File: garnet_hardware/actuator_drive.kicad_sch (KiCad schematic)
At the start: 8 parts, among them J10 Conn_01x02_Pin, Q1 Q_NMOS, Q2 Q_NMOS, Q3 Q_NMOS, Q4 Q_NMOS

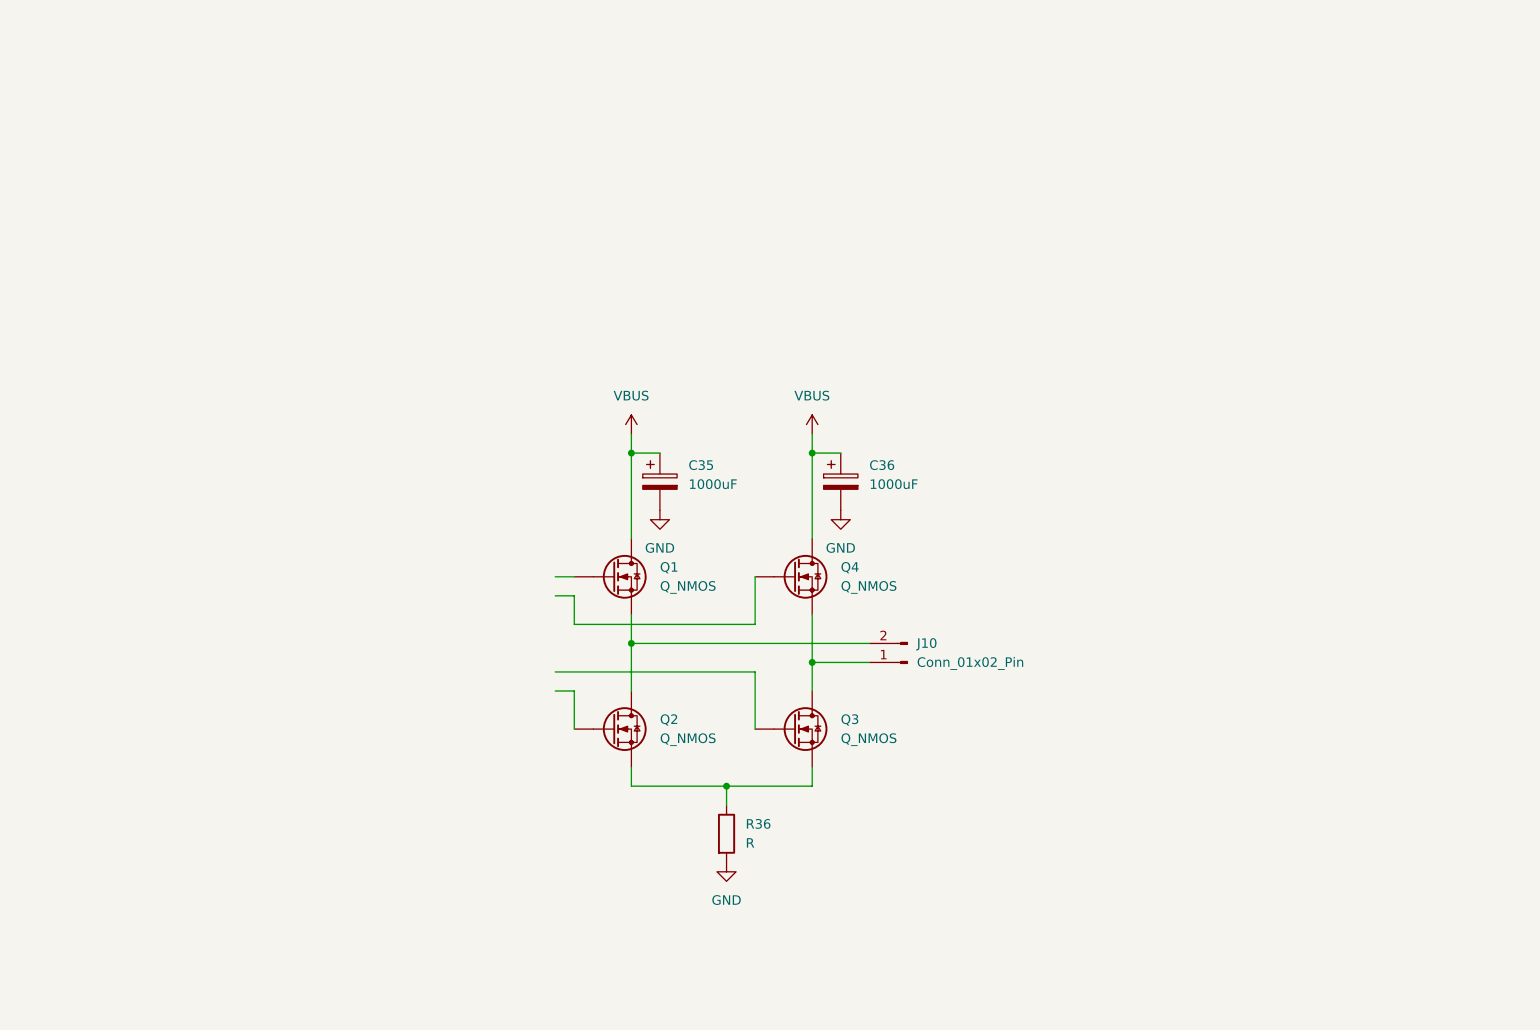
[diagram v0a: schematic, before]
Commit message: added part numbers for H-bridge, started on PCB layout
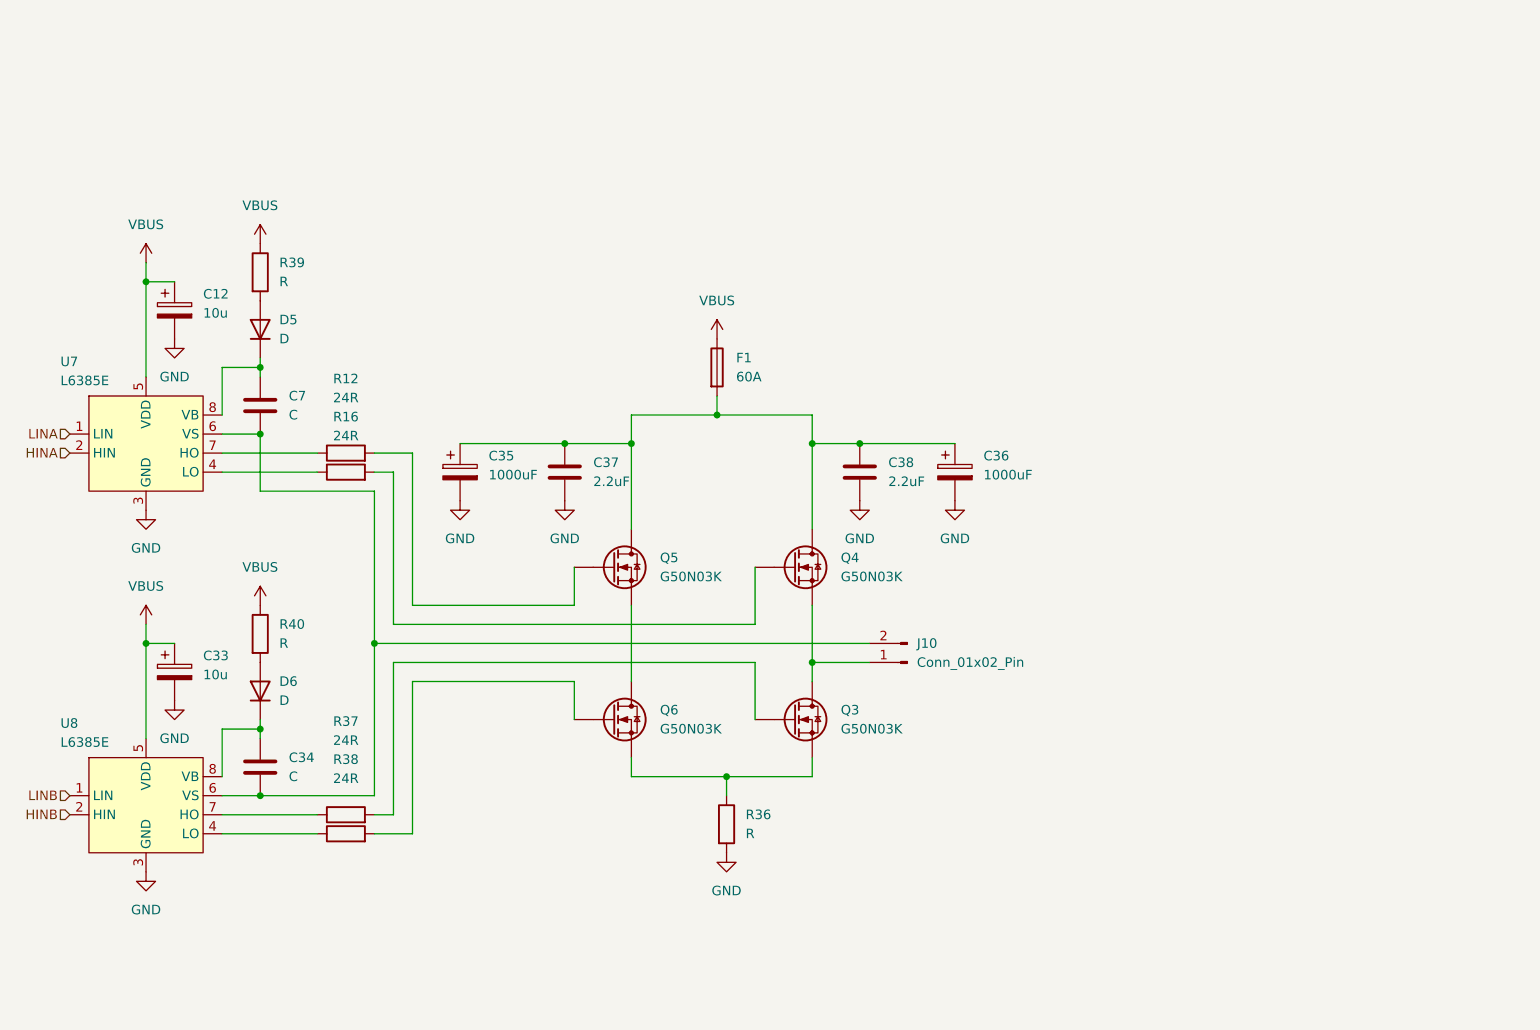
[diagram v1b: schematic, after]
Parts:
- removed Q1, Q2: Q_NMOS, symbol Device:Q_NMOS
- added C12, C33: 10u, symbol Device:C_Polarized
- added C34, C7: C, symbol Device:C
- added C37, C38: 2.2uF, Capacitor_SMD:C_0603_1608Metric_Pad1.08x0.95mm_HandSolder, symbol Device:C
- added D5, D6: D, symbol Device:D
- added F1: 60A, symbol Device:Fuse
- added Q5, Q6: G50N03K, Package_TO_SOT_SMD:TO-252-2, symbol Device:Q_NMOS
- added R12, R16, R37, R38: 24R, Resistor_SMD:R_0603_1608Metric_Pad0.98x0.95mm_HandSolder, symbol Device:R
- added R39, R40: R, Resistor_SMD:R_0603_1608Metric_Pad0.98x0.95mm_HandSolder, symbol Device:R
- added U7, U8: L6385E, Package_SO:SOIC-8_5.3x5.3mm_P1.27mm, symbol customparts:L6385E
- Q3, Q4: value Q_NMOS -> G50N03K; footprint (none) -> Package_TO_SOT_SMD:TO-252-2
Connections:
- net GND: now also C12.2, C33.2, C37.2, C38.2, U7.3 (GND), U8.3 (GND)
- net VBUS: now also C12.1, C33.1, F1.1, R39.1, R40.1, U7.5 (VDD), U8.5 (VDD); no longer C35.1, C36.1, Q4.D
- net at J10.2 (Pin_2): now also C34.2, C7.2, U7.6 (VS), U8.6 (VS)
- net at R36.1: now also Q3.3 (S), Q6.3 (S); no longer Q3.S
- new net: C35.1, C36.1, C37.1, C38.1, F1.2, Q4.2 (D), Q5.2 (D)
- new net: C34.1, D6.1 (K), U8.8 (VB)
- new net: D6.2 (A), R40.2
- new net: D5.2 (A), R39.2
- new net: R16.1, U7.4 (LO)
- new net: R12.1, U7.7 (HO)
- new net: C7.1, D5.1 (K), U7.8 (VB)
- new net: R37.1, U8.7 (HO)
- new net: Q3.1 (G), R37.2
- new net: Q4.1 (G), R16.2
- new net: Q5.1 (G), R12.2
- new net: Q5.3 (S), Q6.2 (D)
- new net: R38.1, U8.4 (LO)
- new net: Q6.1 (G), R38.2
- new net: J10.1 (Pin_1), Q3.2 (D), Q4.3 (S)
- new net HINA: U7.2 (HIN)
- new net HINB: U8.2 (HIN)
- new net LINA: U7.1 (LIN)
- new net LINB: U8.1 (LIN)
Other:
- moved on the sheet: C35, C36, Q3, R36

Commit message: power frount end and sd card layed out on PCB
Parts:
- removed F1: 60A, symbol Device:Fuse
- C12: footprint (none) -> Capacitor_SMD:CP_Elec_4x4.5
- C33: value 10u -> 10uF; footprint (none) -> Capacitor_SMD:CP_Elec_4x4.5
- C34, C7: value C -> 1u; footprint (none) -> Capacitor_SMD:C_0603_1608Metric_Pad1.08x0.95mm_HandSolder
- D5, D6: footprint (none) -> Diode_SMD:D_0603_1608Metric_Pad1.05x0.95mm_HandSolder
- J10: footprint (none) -> Connector_AMASS:AMASS_XT60PW-F_1x02_P7.20mm_Horizontal
- R36: footprint (none) -> Resistor_SMD:R_1020_2550Metric_Pad1.33x5.20mm_HandSolder
- R39, R40: value R -> 5R
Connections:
- net VBUS: now also C35.1, C36.1, C37.1, C38.1, Q4.2 (D), Q5.2 (D)
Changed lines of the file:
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@@
 			)
 		)
-		(property "Footprint" ""
+		(property "Footprint" "Diode_SMD:D_0603_1608Metric_Pad1.05x0.95mm_HandSolder"
 			(at 73.66 105.41 0)
 			(hide yes)
@@
 			)
 		)
-		(property "Value" "R"
+		(property "Value" "5R"
 			(at 76.2 50.7999 0)
 			(show_name no)
@@
 			)
 		)
-		(property "Value" "C"
+		(property "Value" "1u"
 			(at 77.47 116.8399 0)
 			(show_name no)
@@
 			)
 		)
-		(property "Footprint" ""
+		(property "Footprint" "Capacitor_SMD:C_0603_1608Metric_Pad1.08x0.95mm_HandSolder"
 			(at 74.6252 119.38 0)
 			(hide yes)
@@
 	(symbol
 		(lib_id "power:VBUS")
-		(at 134.62 58.42 0)
+		(at 134.62 66.04 0)
 		(unit 1)
 		(body_style 1)
@@
 		(fields_autoplaced yes)
 		(property "Reference" "#PWR073"
-			(at 134.62 62.23 0)
+			(at 134.62 69.85 0)
 			(hide yes)
 			(show_name no)
@@
 		)
 		(property "Value" "VBUS"
-			(at 134.62 53.34 0)
+			(at 134.62 60.96 0)
 			(show_name no)
 			(do_not_autoplace no)
@@
 		)
 		(property "Footprint" ""
-			(at 134.62 58.42 0)
+			(at 134.62 66.04 0)
 			(hide yes)
 			(show_name no)
@@
 		)
 		(property "Datasheet" ""
-			(at 134.62 58.42 0)
+			(at 134.62 66.04 0)
 			(hide yes)
 			(show_name no)
@@
 		)
 		(property "Description" "Power symbol creates a global label with name \"VBUS\""
-			(at 134.62 58.42 0)
+			(at 134.62 66.04 0)
 			(hide yes)
 			(show_name no)
@@
 			)
 		)
-		(property "Value" "C"
+		(property "Value" "1u"
 			(at 77.47 68.5799 0)
 			(show_name no)
@@
 			)
 		)
-		(property "Footprint" ""
+		(property "Footprint" "Capacitor_SMD:C_0603_1608Metric_Pad1.08x0.95mm_HandSolder"
 			(at 74.6252 71.12 0)
 			(hide yes)
@@
 			)
 		)
-		(property "Footprint" ""
+		(property "Footprint" "Resistor_SMD:R_1020_2550Metric_Pad1.33x5.20mm_HandSolder"
 			(at 134.112 123.19 90)
 			(hide yes)
@@
 			)
 		)
-		(property "Footprint" ""
+		(property "Footprint" "Capacitor_SMD:CP_Elec_4x4.5"
 			(at 63.1952 58.42 0)
 			(hide yes)
@@
 			)
 		)
-		(property "Footprint" ""
+		(property "Footprint" "Diode_SMD:D_0603_1608Metric_Pad1.05x0.95mm_HandSolder"
 			(at 73.66 57.15 0)
 			(hide yes)
@@
 			)
 		)
-		(property "Value" "10u"
+		(property "Value" "10uF"
 			(at 66.04 103.2509 0)
 			(show_name no)
@@
 			)
 		)
-		(property "Footprint" ""
+		(property "Footprint" "Capacitor_SMD:CP_Elec_4x4.5"
 			(at 63.1952 106.68 0)
 			(hide yes)
@@
 			)
 		)
-		(property "Value" "R"
+		(property "Value" "5R"
 			(at 76.2 99.0599 0)
 			(show_name no)
@@
 	)
 	(symbol
-		(lib_id "Device:Fuse")
-		(at 134.62 62.23 0)
-		(unit 1)
-		(body_style 1)
-		(exclude_from_sim no)
-		(in_bom yes)
-		(on_board yes)
-		(in_pos_files yes)
-		(dnp no)
-		(fields_autoplaced yes)
-		(property "Reference" "F1"
-			(at 137.16 60.9599 0)
-			(show_name no)
-			(do_not_autoplace no)
-			(effects
-				(font
-					(size 1.27 1.27)
-				)
-				(justify left)
-			)
-		)
-		(property "Value" "60A"
-			(at 137.16 63.4999 0)
-			(show_name no)
-			(do_not_autoplace no)
-			(effects
-				(font
-					(size 1.27 1.27)
-				)
-				(justify left)
-			)
-		)
-		(property "Footprint" ""
-			(at 132.842 62.23 90)
-			(hide yes)
-			(show_name no)
-			(do_not_autoplace no)
-			(effects
-				(font
-					(size 1.27 1.27)
-				)
-			)
-		)
-		(property "Datasheet" ""
-			(at 134.62 62.23 0)
-			(hide yes)
-			(show_name no)
-			(do_not_autoplace no)
-			(effects
-				(font
-					(size 1.27 1.27)
-				)
-			)
-		)
-		(property "Description" "Fuse"
-			(at 134.62 62.23 0)
-			(hide yes)
-			(show_name no)
-			(do_not_autoplace no)
-			(effects
-				(font
-					(size 1.27 1.27)
-				)
-			)
-		)
-		(pin "1"
-		)
-		(pin "2"
-		)
-		(instances
-			(project "garnet"
-				(path "/d9f850a7-c985-4ceb-9739-25f51398aa81/cdd7dad9-2a17-44d2-a1dd-93d1e8942a69"
-					(reference "F1")
-					(unit 1)
-				)
-			)
-		)
-	)
-	(symbol
 		(lib_id "customparts:L6385E")
 		(at 49.53 121.92 0)
@@
 			)
 		)
-		(property "Footprint" ""
+		(property "Footprint" "Connector_AMASS:AMASS_XT60PW-F_1x02_P7.20mm_Horizontal"
 			(at 160.02 101.6 0)
 			(hide yes)

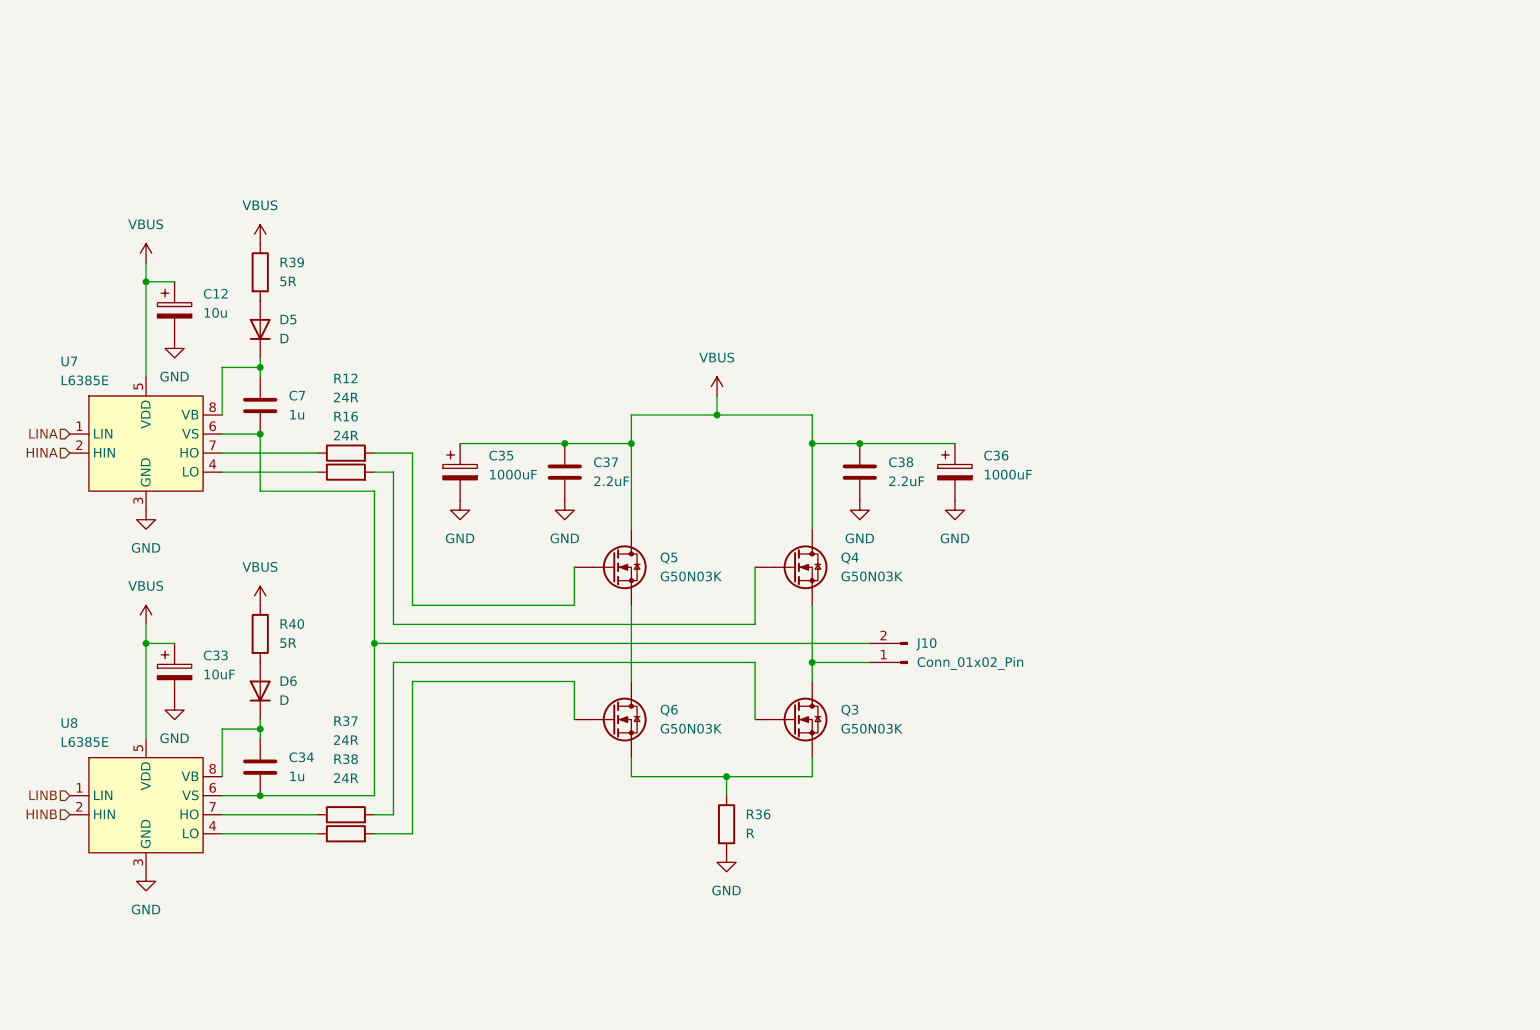
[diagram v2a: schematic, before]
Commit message: cleaned SPI lines, replaced MOSFETS with more sutible ones, added free wheeling diodes added current sensing
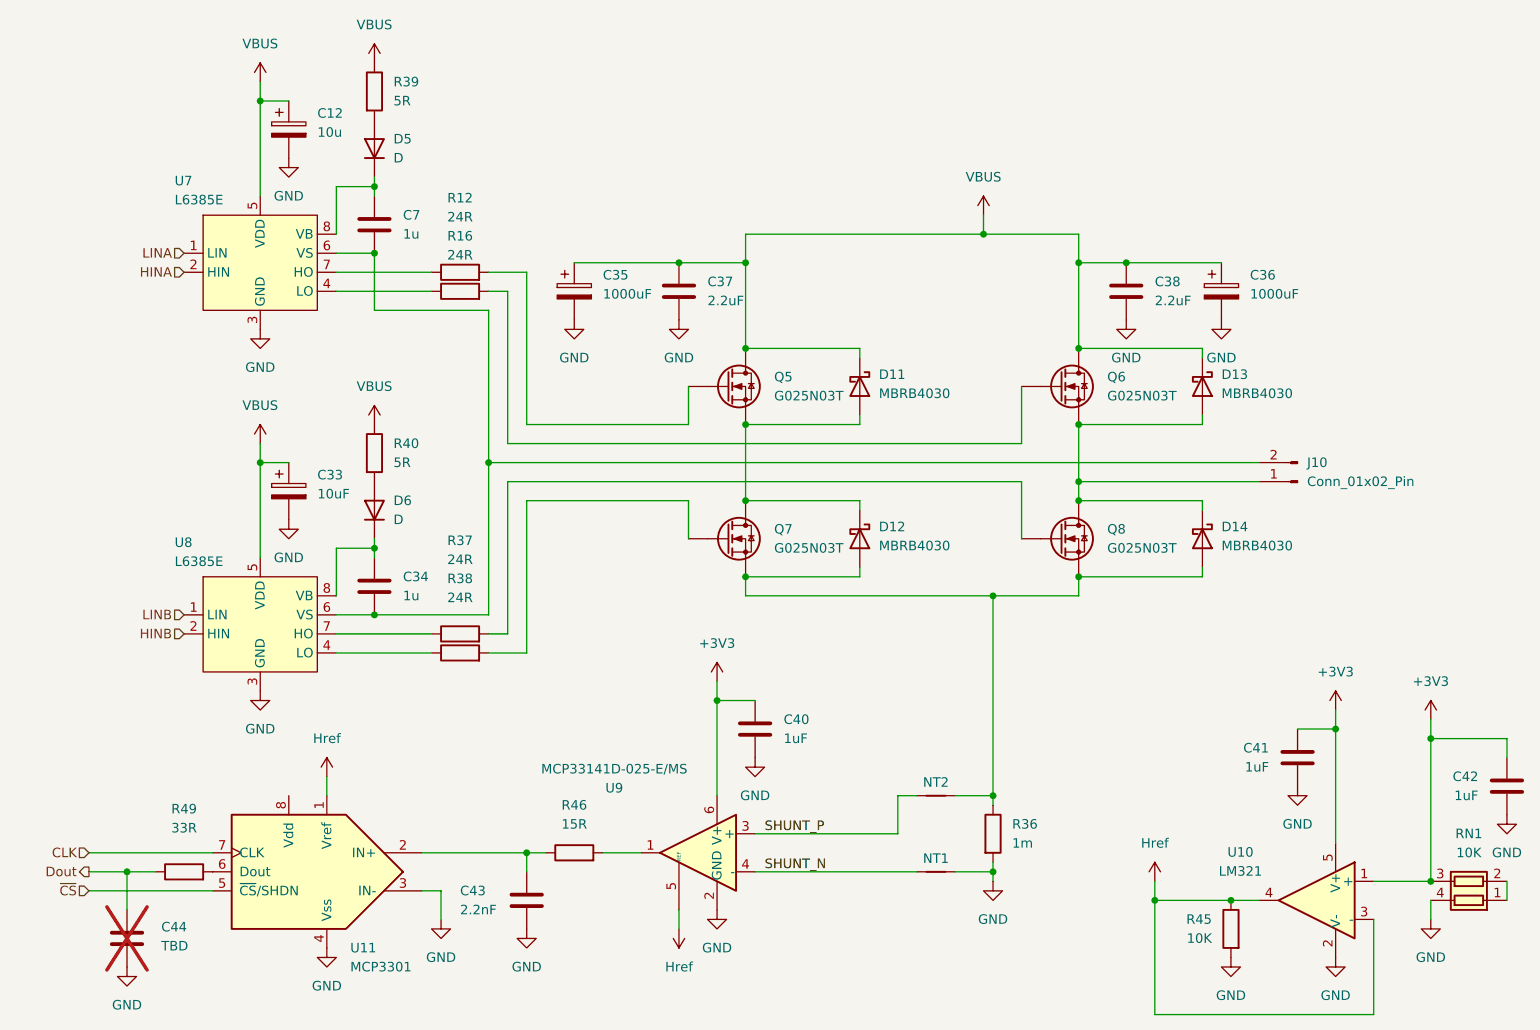
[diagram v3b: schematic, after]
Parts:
- removed Q3, Q4: G50N03K, Package_TO_SOT_SMD:TO-252-2, symbol Device:Q_NMOS
- added C40, C41, C42: 1uF, Capacitor_SMD:C_0603_1608Metric_Pad1.08x0.95mm_HandSolder, symbol Device:C
- added C43: 2.2nF, Capacitor_SMD:C_0603_1608Metric_Pad1.08x0.95mm_HandSolder, symbol Device:C
- added C44: TBD, Capacitor_SMD:C_0603_1608Metric_Pad1.08x0.95mm_HandSolder, symbol Device:C
- added D11, D12, D13, D14: MBRB4030, Package_TO_SOT_SMD:TO-263-2, symbol Device:D_Schottky
- added NT1, NT2: (no value), symbol Device:NetTie_2
- added Q7, Q8: G025N03T, Package_TO_SOT_THT:TO-220-3_Vertical, symbol Device:Q_NMOS
- added R45: 10K, symbol Device:R
- added R46: 15R, Resistor_SMD:R_0603_1608Metric_Pad0.98x0.95mm_HandSolder, symbol Device:R
- added R49: 33R, Resistor_SMD:R_0603_1608Metric_Pad0.98x0.95mm_HandSolder, symbol Device:R
- added RN1: 10K, Resistor_SMD:R_Array_Convex_2x0606, symbol Device:R_Pack02
- added U10: LM321, Package_TO_SOT_SMD:SOT-23-5, symbol Amplifier_Operational:LM321
- added U11: MCP3301, symbol Analog_ADC:MCP3301
- added U9: MCP33141D-025-E/MS, Package_SO:MSOP-10_3x3mm_P0.5mm, symbol Amplifier_Current:INA181
- Q5, Q6: value G50N03K -> G025N03T; footprint Package_TO_SOT_SMD:TO-252-2 -> Package_TO_SOT_THT:TO-220-3_Vertical
- R36: value R -> 1m; footprint Resistor_SMD:R_1020_2550Metric_Pad1.33x5.20mm_HandSolder -> Resistor_SMD:R_2512_6332Metric_Pad1.40x3.35mm_HandSolder
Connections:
- net GND: now also C40.1, C41.1, C42.1, C43.2, C44.2, NT1.2, R45.2, RN1.4 (R1.2), U10.2 (V-), U11.3 (IN-), U11.4 (Vss), U9.2 (GND)
- net VBUS: now also Q6.2 (D), D11.1 (K), D13.1 (K)
- net at R37.2: now also Q8.1 (G)
- net at R16.2: now also Q6.1 (G)
- net at Q5.3 (S): now also D11.2 (A), D12.1 (K), Q7.2 (D); no longer Q6.2 (D)
- net at R36.1: now also D12.2 (A), D14.2 (A), NT2.2, Q7.3 (S), Q8.3 (S); no longer Q6.3 (S)
- net at R38.2: now also Q7.1 (G); no longer Q6.1 (G)
- net at J10.1 (Pin_1): now also Q6.3 (S), D13.2 (A), D14.1 (K), Q8.2 (D)
- new net: R46.2, U9.1
- new net: C43.1, R46.1, U11.2 (IN+)
- new net: R49.2, U11.6 (Dout)
- new net: RN1.1 (R1.1), RN1.2 (R2.1)
- new net +3V3: C40.2, C41.2, C42.2, RN1.3 (R2.2), U10.1 (+), U10.5 (V+), U9.6 (V+)
- new net CLK: U11.7 (CLK)
- new net Dout: C44.1, R49.1
- new net Href: R45.1, U10.3 (-), U10.4, U11.1 (Vref), U9.5 (REF)
- new net SHUNT_N: NT1.1, U9.4 (-)
- new net SHUNT_P: NT2.1, U9.3 (+)
- new net ~{CS}: U11.5 (~{CS}/SHDN)
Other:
- moved on the sheet: C12, C33, C34, C35, C36, C37, C38, C7, D5, D6, J10, Q5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
